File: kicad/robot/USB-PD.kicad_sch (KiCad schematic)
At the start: 38 parts, among them U11 MAX77958EWV+T

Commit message: Assigned resistor footprints
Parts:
- R32, R33: footprint (none) -> Resistor_SMD:R_0402_1005Metric
- R34, R35, R36, R37, R38, R39, R40: footprint (none) -> Resistor_SMD:R_0603_1608Metric
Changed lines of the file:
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@@
       (effects (font (size 1.27 1.27)) (justify left))
     )
-    (property "Footprint" "" (id 2) (at 314.452 171.45 90)
+    (property "Footprint" "Resistor_SMD:R_0603_1608Metric" (id 2) (at 314.452 171.45 90)
       (effects (font (size 1.27 1.27)) hide)
     )
@@
     (property "Reference" "R32" (id 0) (at 200.66 205.74 90))
     (property "Value" "1" (id 1) (at 200.66 208.28 90))
-    (property "Footprint" "" (id 2) (at 200.66 213.868 90)
+    (property "Footprint" "Resistor_SMD:R_0402_1005Metric" (id 2) (at 200.66 213.868 90)
       (effects (font (size 1.27 1.27)) hide)
     )
@@
       (effects (font (size 1.27 1.27)) (justify left))
     )
-    (property "Footprint" "" (id 2) (at 336.042 213.36 90)
+    (property "Footprint" "Resistor_SMD:R_0603_1608Metric" (id 2) (at 336.042 213.36 90)
       (effects (font (size 1.27 1.27)) hide)
     )
@@
       (effects (font (size 1.27 1.27)) (justify left))
     )
-    (property "Footprint" "" (id 2) (at 355.092 270.51 90)
+    (property "Footprint" "Resistor_SMD:R_0603_1608Metric" (id 2) (at 355.092 270.51 90)
       (effects (font (size 1.27 1.27)) hide)
     )
@@
       (effects (font (size 1.27 1.27)) (justify left))
     )
-    (property "Footprint" "" (id 2) (at 323.342 171.45 90)
+    (property "Footprint" "Resistor_SMD:R_0603_1608Metric" (id 2) (at 323.342 171.45 90)
       (effects (font (size 1.27 1.27)) hide)
     )
@@
     (property "Reference" "R33" (id 0) (at 200.66 222.25 90))
     (property "Value" "1" (id 1) (at 200.66 219.71 90))
-    (property "Footprint" "" (id 2) (at 200.66 218.948 90)
+    (property "Footprint" "Resistor_SMD:R_0402_1005Metric" (id 2) (at 200.66 218.948 90)
       (effects (font (size 1.27 1.27)) hide)
     )
@@
       (effects (font (size 1.27 1.27)) (justify left))
     )
-    (property "Footprint" "" (id 2) (at 341.122 270.51 90)
+    (property "Footprint" "Resistor_SMD:R_0603_1608Metric" (id 2) (at 341.122 270.51 90)
       (effects (font (size 1.27 1.27)) hide)
     )
@@
       (effects (font (size 1.27 1.27)) (justify left))
     )
-    (property "Footprint" "" (id 2) (at 341.122 256.54 90)
+    (property "Footprint" "Resistor_SMD:R_0603_1608Metric" (id 2) (at 341.122 256.54 90)
       (effects (font (size 1.27 1.27)) hide)
     )
@@
       (effects (font (size 1.27 1.27)) (justify left))
     )
-    (property "Footprint" "" (id 2) (at 355.092 256.54 90)
-      (effects (font (size 1.27 1.27)) hide)
-    )
+    (property "Footprint" "Resistor_SMD:R_0603_1608Metric" (id 2) (at 355.092 256.54 90)
+      (effects (font (size 1.27 1.27)) hide)
+    )

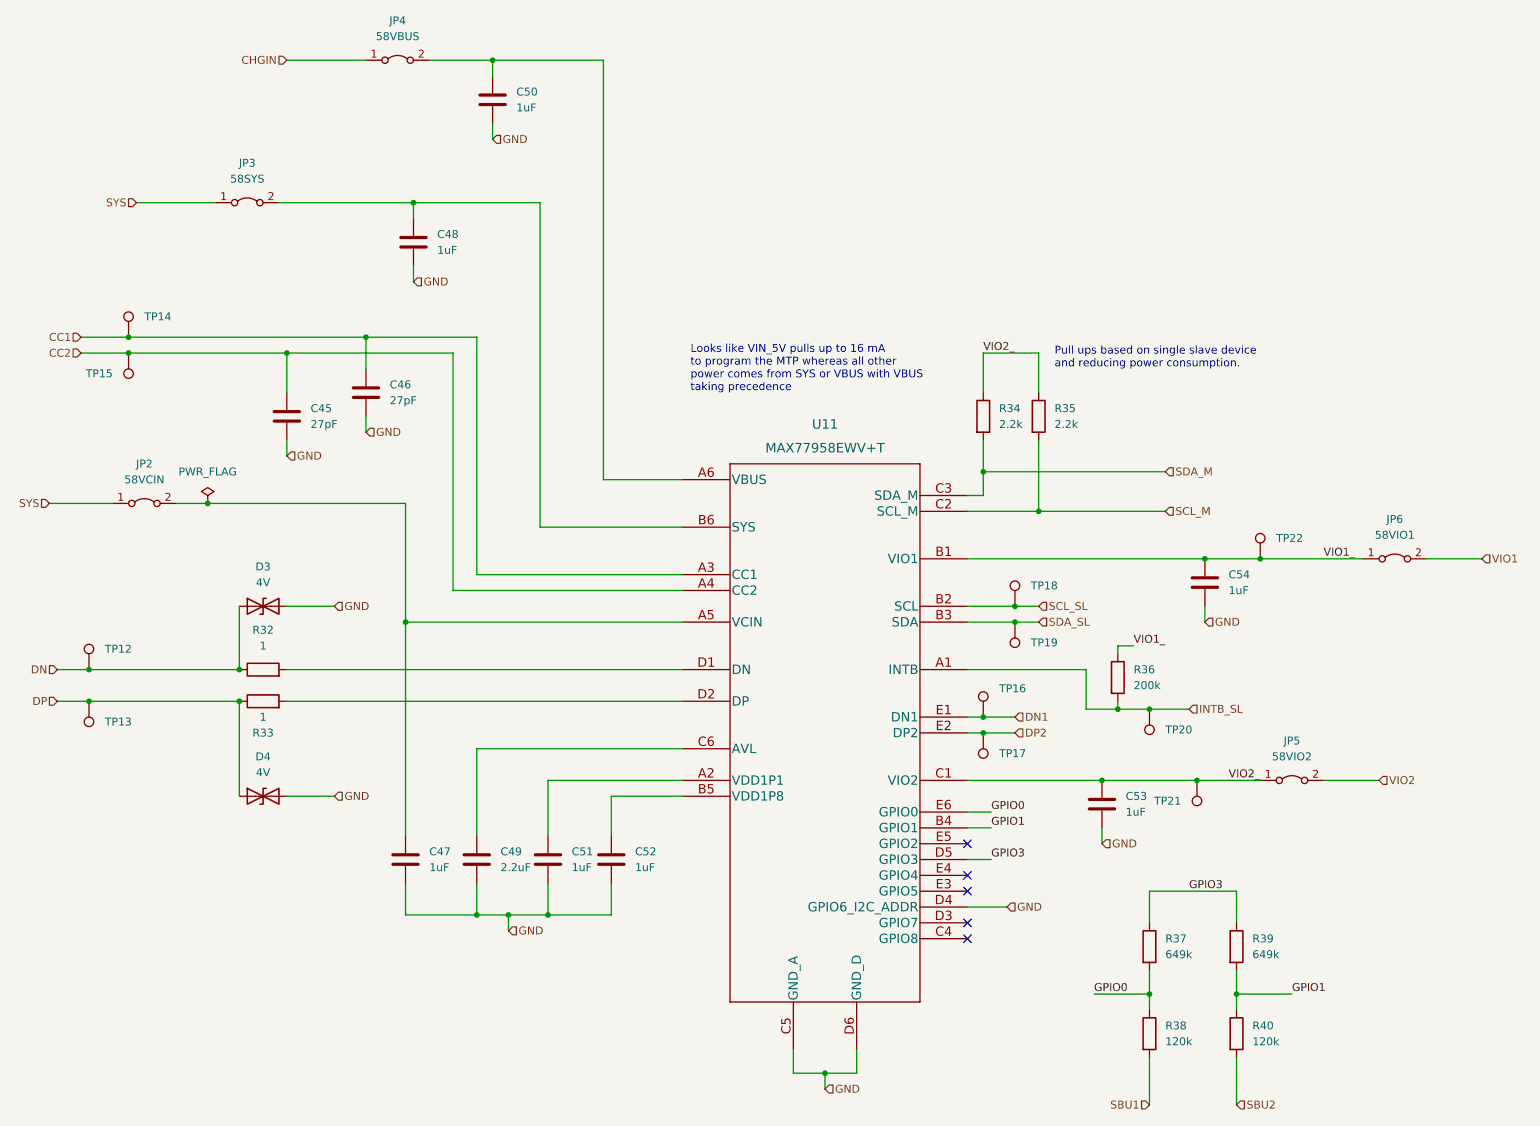
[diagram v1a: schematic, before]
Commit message: Assigned capacitor footprints
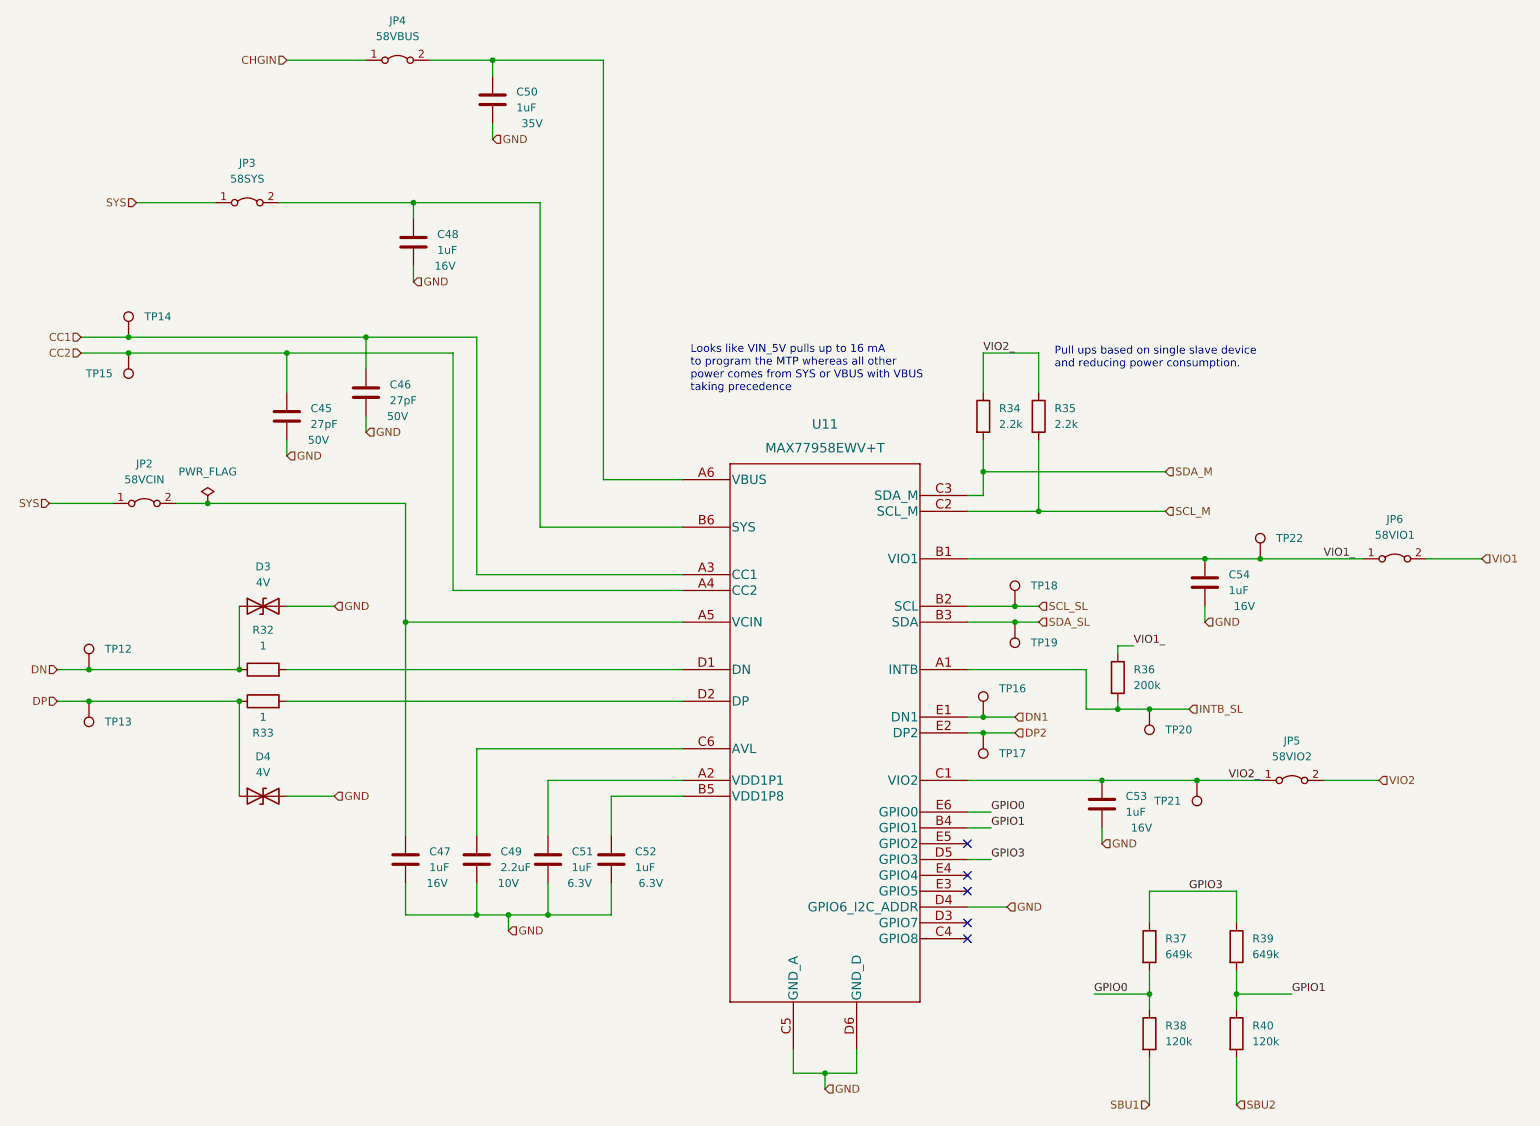
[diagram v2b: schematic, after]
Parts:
- C45, C46: footprint (none) -> Capacitor_SMD:C_0402_1005Metric
- C47, C48, C50: footprint (none) -> Capacitor_SMD:C_0805_2012Metric
- C49, C51, C52, C53, C54: footprint (none) -> Capacitor_SMD:C_0603_1608Metric
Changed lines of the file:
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@@
   )
   (symbol (lib_id "Device:C") (at 217.17 167.64 0) (unit 1)
-    (in_bom yes) (on_board yes) (fields_autoplaced)
+    (in_bom yes) (on_board yes)
     (property "Reference" "C46" (id 0) (at 220.98 166.3699 0)
       (effects (font (size 1.27 1.27)) (justify left))
@@
       (effects (font (size 1.27 1.27)) (justify left))
     )
-    (property "Footprint" "" (id 2) (at 218.1352 171.45 0)
+    (property "Footprint" "Capacitor_SMD:C_0402_1005Metric" (id 2) (at 218.1352 171.45 0)
       (effects (font (size 1.27 1.27)) hide)
     )
@@
       (effects (font (size 1.27 1.27)) hide)
     )
-    (property "Description" "50V" (id 4) (at 217.17 167.64 0)
-      (effects (font (size 1.27 1.27)) hide)
-    )
+    (property "Description" "50V" (id 4) (at 222.25 171.45 0))
     (pin "1")
     (pin "2")
@@
   )
   (symbol (lib_id "Device:C") (at 335.28 233.68 0) (unit 1)
-    (in_bom yes) (on_board yes) (fields_autoplaced)
+    (in_bom yes) (on_board yes)
     (property "Reference" "C53" (id 0) (at 339.09 232.4099 0)
       (effects (font (size 1.27 1.27)) (justify left))
@@
       (effects (font (size 1.27 1.27)) (justify left))
     )
-    (property "Footprint" "" (id 2) (at 336.2452 237.49 0)
+    (property "Footprint" "Capacitor_SMD:C_0603_1608Metric" (id 2) (at 336.2452 237.49 0)
       (effects (font (size 1.27 1.27)) hide)
     )
@@
       (effects (font (size 1.27 1.27)) hide)
     )
-    (property "Description" "16V" (id 4) (at 335.28 233.68 0)
-      (effects (font (size 1.27 1.27)) hide)
-    )
+    (property "Description" "16V" (id 4) (at 341.63 237.49 0))
     (pin "1")
     (pin "2")
@@
   )
   (symbol (lib_id "Device:C") (at 256.54 242.57 0) (unit 1)
-    (in_bom yes) (on_board yes) (fields_autoplaced)
+    (in_bom yes) (on_board yes)
     (property "Reference" "C52" (id 0) (at 260.35 241.2999 0)
       (effects (font (size 1.27 1.27)) (justify left))
@@
       (effects (font (size 1.27 1.27)) (justify left))
     )
-    (property "Footprint" "" (id 2) (at 257.5052 246.38 0)
+    (property "Footprint" "Capacitor_SMD:C_0603_1608Metric" (id 2) (at 257.5052 246.38 0)
       (effects (font (size 1.27 1.27)) hide)
     )
@@
       (effects (font (size 1.27 1.27)) hide)
     )
-    (property "Description" "6.3V" (id 4) (at 256.54 242.57 0)
-      (effects (font (size 1.27 1.27)) hide)
-    )
+    (property "Description" "6.3V" (id 4) (at 262.89 246.38 0))
     (pin "1")
     (pin "2")
   )
   (symbol (lib_id "Device:C") (at 224.79 143.51 0) (unit 1)
-    (in_bom yes) (on_board yes) (fields_autoplaced)
+    (in_bom yes) (on_board yes)
     (property "Reference" "C48" (id 0) (at 228.6 142.2399 0)
       (effects (font (size 1.27 1.27)) (justify left))
@@
       (effects (font (size 1.27 1.27)) (justify left))
     )
-    (property "Footprint" "" (id 2) (at 225.7552 147.32 0)
+    (property "Footprint" "Capacitor_SMD:C_0805_2012Metric" (id 2) (at 225.7552 147.32 0)
       (effects (font (size 1.27 1.27)) hide)
     )
@@
       (effects (font (size 1.27 1.27)) hide)
     )
-    (property "Description" "35V" (id 4) (at 224.79 143.51 0)
-      (effects (font (size 1.27 1.27)) hide)
-    )
+    (property "Description" "16V" (id 4) (at 229.87 147.32 0))
     (pin "1")
     (pin "2")
@@
   )
   (symbol (lib_id "Device:C") (at 223.52 242.57 0) (unit 1)
-    (in_bom yes) (on_board yes) (fields_autoplaced)
+    (in_bom yes) (on_board yes)
     (property "Reference" "C47" (id 0) (at 227.33 241.2999 0)
       (effects (font (size 1.27 1.27)) (justify left))
@@
       (effects (font (size 1.27 1.27)) (justify left))
     )
-    (property "Footprint" "" (id 2) (at 224.4852 246.38 0)
+    (property "Footprint" "Capacitor_SMD:C_0805_2012Metric" (id 2) (at 224.4852 246.38 0)
       (effects (font (size 1.27 1.27)) hide)
     )
@@
       (effects (font (size 1.27 1.27)) hide)
     )
-    (property "Description" "16V" (id 4) (at 223.52 242.57 0)
-      (effects (font (size 1.27 1.27)) hide)
-    )
+    (property "Description" "16V" (id 4) (at 228.6 246.38 0))
     (pin "1")
     (pin "2")
@@
   )
   (symbol (lib_id "Device:C") (at 204.47 171.45 0) (unit 1)
-    (in_bom yes) (on_board yes) (fields_autoplaced)
+    (in_bom yes) (on_board yes)
     (property "Reference" "C45" (id 0) (at 208.28 170.1799 0)
       (effects (font (size 1.27 1.27)) (justify left))
@@
       (effects (font (size 1.27 1.27)) (justify left))
     )
-    (property "Footprint" "" (id 2) (at 205.4352 175.26 0)
+    (property "Footprint" "Capacitor_SMD:C_0402_1005Metric" (id 2) (at 205.4352 175.26 0)
       (effects (font (size 1.27 1.27)) hide)
     )
@@
       (effects (font (size 1.27 1.27)) hide)
     )
-    (property "Description" "50V" (id 4) (at 204.47 171.45 0)
-      (effects (font (size 1.27 1.27)) hide)
-    )
+    (property "Description" "50V" (id 4) (at 209.55 175.26 0))
     (pin "1")
     (pin "2")
@@
   )
   (symbol (lib_id "Device:C") (at 237.49 120.65 0) (unit 1)
-    (in_bom yes) (on_board yes) (fields_autoplaced)
+    (in_bom yes) (on_board yes)
     (property "Reference" "C50" (id 0) (at 241.3 119.3799 0)
       (effects (font (size 1.27 1.27)) (justify left))
@@
       (effects (font (size 1.27 1.27)) (justify left))
     )
-    (property "Footprint" "" (id 2) (at 238.4552 124.46 0)
+    (property "Footprint" "Capacitor_SMD:C_0805_2012Metric" (id 2) (at 238.4552 124.46 0)
       (effects (font (size 1.27 1.27)) hide)
     )
@@
       (effects (font (size 1.27 1.27)) hide)
     )
-    (property "Description" "35V" (id 4) (at 237.49 120.65 0)
-      (effects (font (size 1.27 1.27)) hide)
-    )
+    (property "Description" "35V" (id 4) (at 243.84 124.46 0))
     (pin "1")
     (pin "2")
@@
   )
   (symbol (lib_id "Device:C") (at 351.79 198.12 0) (unit 1)
-    (in_bom yes) (on_board yes) (fields_autoplaced)
+    (in_bom yes) (on_board yes)
     (property "Reference" "C54" (id 0) (at 355.6 196.8499 0)
       (effects (font (size 1.27 1.27)) (justify left))
@@
       (effects (font (size 1.27 1.27)) (justify left))
     )
-    (property "Footprint" "" (id 2) (at 352.7552 201.93 0)
+    (property "Footprint" "Capacitor_SMD:C_0603_1608Metric" (id 2) (at 352.7552 201.93 0)
       (effects (font (size 1.27 1.27)) hide)
     )
@@
       (effects (font (size 1.27 1.27)) hide)
     )
-    (property "Description" "16V" (id 4) (at 351.79 198.12 0)
-      (effects (font (size 1.27 1.27)) hide)
-    )
+    (property "Description" "16V" (id 4) (at 358.14 201.93 0))
     (pin "1")
     (pin "2")
@@
   )
   (symbol (lib_id "Device:C") (at 246.38 242.57 0) (unit 1)
-    (in_bom yes) (on_board yes) (fields_autoplaced)
+    (in_bom yes) (on_board yes)
     (property "Reference" "C51" (id 0) (at 250.19 241.2999 0)
       (effects (font (size 1.27 1.27)) (justify left))
@@
       (effects (font (size 1.27 1.27)) (justify left))
     )
-    (property "Footprint" "" (id 2) (at 247.3452 246.38 0)
+    (property "Footprint" "Capacitor_SMD:C_0603_1608Metric" (id 2) (at 247.3452 246.38 0)
       (effects (font (size 1.27 1.27)) hide)
     )
@@
       (effects (font (size 1.27 1.27)) hide)
     )
-    (property "Description" "6.3V" (id 4) (at 246.38 242.57 0)
-      (effects (font (size 1.27 1.27)) hide)
-    )
+    (property "Description" "6.3V" (id 4) (at 251.46 246.38 0))
     (pin "1")
     (pin "2")
   )
   (symbol (lib_id "Device:C") (at 234.95 242.57 0) (unit 1)
-    (in_bom yes) (on_board yes) (fields_autoplaced)
+    (in_bom yes) (on_board yes)
     (property "Reference" "C49" (id 0) (at 238.76 241.2999 0)
       (effects (font (size 1.27 1.27)) (justify left))
@@
       (effects (font (size 1.27 1.27)) (justify left))
     )
-    (property "Footprint" "" (id 2) (at 235.9152 246.38 0)
+    (property "Footprint" "Capacitor_SMD:C_0603_1608Metric" (id 2) (at 235.9152 246.38 0)
       (effects (font (size 1.27 1.27)) hide)
     )
@@
       (effects (font (size 1.27 1.27)) hide)
     )
-    (property "Description" "10V" (id 4) (at 234.95 242.57 0)
-      (effects (font (size 1.27 1.27)) hide)
-    )
-    (pin "1")
-    (pin "2")
+    (property "Description" "10V" (id 4) (at 240.03 246.38 0))
+    (pin "1")
+    (pin "2")

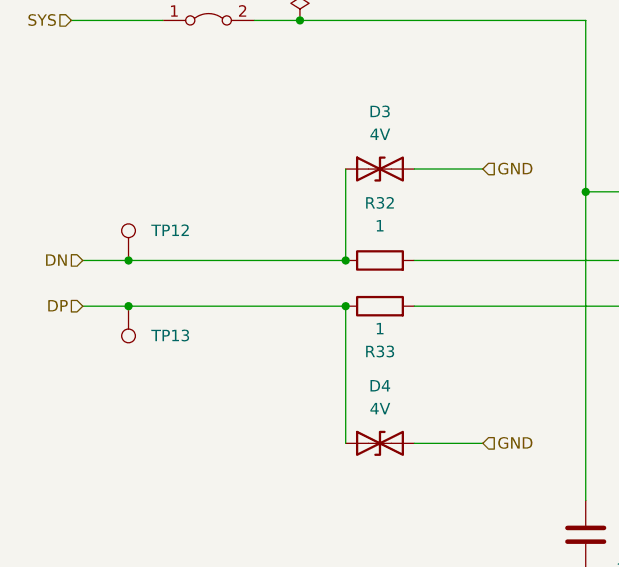
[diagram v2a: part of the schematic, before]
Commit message: removed two duplicate test points
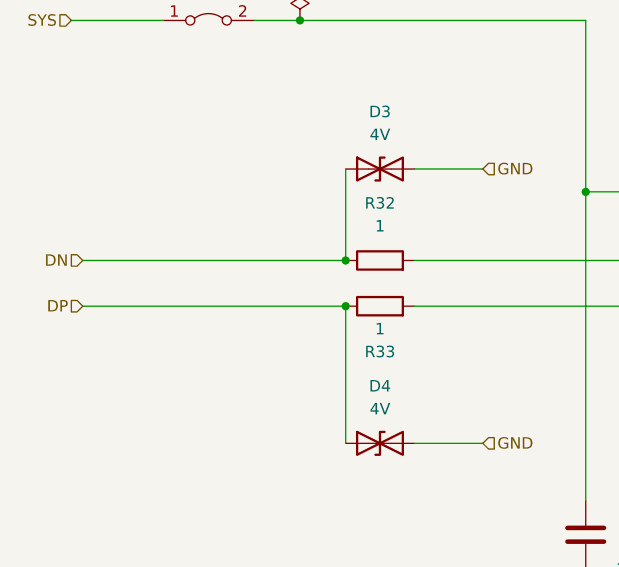
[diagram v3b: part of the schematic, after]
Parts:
- removed TP12, TP13: TestPoint, symbol Connector:TestPoint
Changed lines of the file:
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@@
   (junction (at 179.07 161.29) (diameter 0) (color 0 0 0 0)
   )
-  (junction (at 172.72 217.17) (diameter 0) (color 0 0 0 0)
-  )
   (junction (at 356.87 264.16) (diameter 0) (color 0 0 0 0)
   )
@@
   )
   (junction (at 179.07 158.75) (diameter 0) (color 0 0 0 0)
-  )
-  (junction (at 172.72 212.09) (diameter 0) (color 0 0 0 0)
   )
   (junction (at 321.31 204.47) (diameter 0) (color 0 0 0 0)
@@
     (stroke (width 0) (type default) (color 0 0 0 0))
   )
-  (wire (pts (xy 172.72 212.09) (xy 196.85 212.09))
+  (wire (pts (xy 167.64 212.09) (xy 196.85 212.09))
     (stroke (width 0) (type default) (color 0 0 0 0))
   )
@@
     (stroke (width 0) (type default) (color 0 0 0 0))
   )
-  (wire (pts (xy 172.72 217.17) (xy 196.85 217.17))
+  (wire (pts (xy 167.64 217.17) (xy 196.85 217.17))
     (stroke (width 0) (type default) (color 0 0 0 0))
   )
@@
     (stroke (width 0) (type default) (color 0 0 0 0))
   )
-  (wire (pts (xy 167.64 212.09) (xy 172.72 212.09))
-    (stroke (width 0) (type default) (color 0 0 0 0))
-  )
   (wire (pts (xy 204.47 175.26) (xy 204.47 177.8))
     (stroke (width 0) (type default) (color 0 0 0 0))
@@
   )
   (wire (pts (xy 387.35 194.31) (xy 396.24 194.31))
-    (stroke (width 0) (type default) (color 0 0 0 0))
-  )
-  (wire (pts (xy 167.64 217.17) (xy 172.72 217.17))
     (stroke (width 0) (type default) (color 0 0 0 0))
   )
@@
     (pin "1")
     (pin "2")
-  )
-  (symbol (lib_id "Connector:TestPoint") (at 172.72 212.09 0) (unit 1)
-    (in_bom yes) (on_board yes) (fields_autoplaced)
-    (property "Reference" "TP12" (id 0) (at 175.26 208.7879 0)
-      (effects (font (size 1.27 1.27)) (justify left))
-    )
-    (property "Value" "TestPoint" (id 1) (at 175.26 210.0579 0)
-      (effects (font (size 1.27 1.27)) (justify left) hide)
-    )
-    (property "Footprint" "" (id 2) (at 177.8 212.09 0)
-      (effects (font (size 1.27 1.27)) hide)
-    )
-    (property "Datasheet" "~" (id 3) (at 177.8 212.09 0)
-      (effects (font (size 1.27 1.27)) hide)
-    )
-    (pin "1")
   )
   (symbol (lib_id "Connector:TestPoint") (at 350.52 229.87 0) (mirror x) (unit 1)
@@
     (pin "2")
   )
-  (symbol (lib_id "Connector:TestPoint") (at 172.72 217.17 180) (unit 1)
-    (in_bom yes) (on_board yes) (fields_autoplaced)
-    (property "Reference" "TP13" (id 0) (at 175.26 220.4719 0)
-      (effects (font (size 1.27 1.27)) (justify right))
-    )
-    (property "Value" "TestPoint" (id 1) (at 175.26 221.7419 0)
-      (effects (font (size 1.27 1.27)) (justify right) hide)
-    )
-    (property "Footprint" "" (id 2) (at 167.64 217.17 0)
-      (effects (font (size 1.27 1.27)) hide)
-    )
-    (property "Datasheet" "~" (id 3) (at 167.64 217.17 0)
-      (effects (font (size 1.27 1.27)) hide)
-    )
-    (pin "1")
-  )
   (symbol (lib_id "Device:R") (at 342.9 270.51 0) (unit 1)
